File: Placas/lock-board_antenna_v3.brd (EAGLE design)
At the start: 7 parts

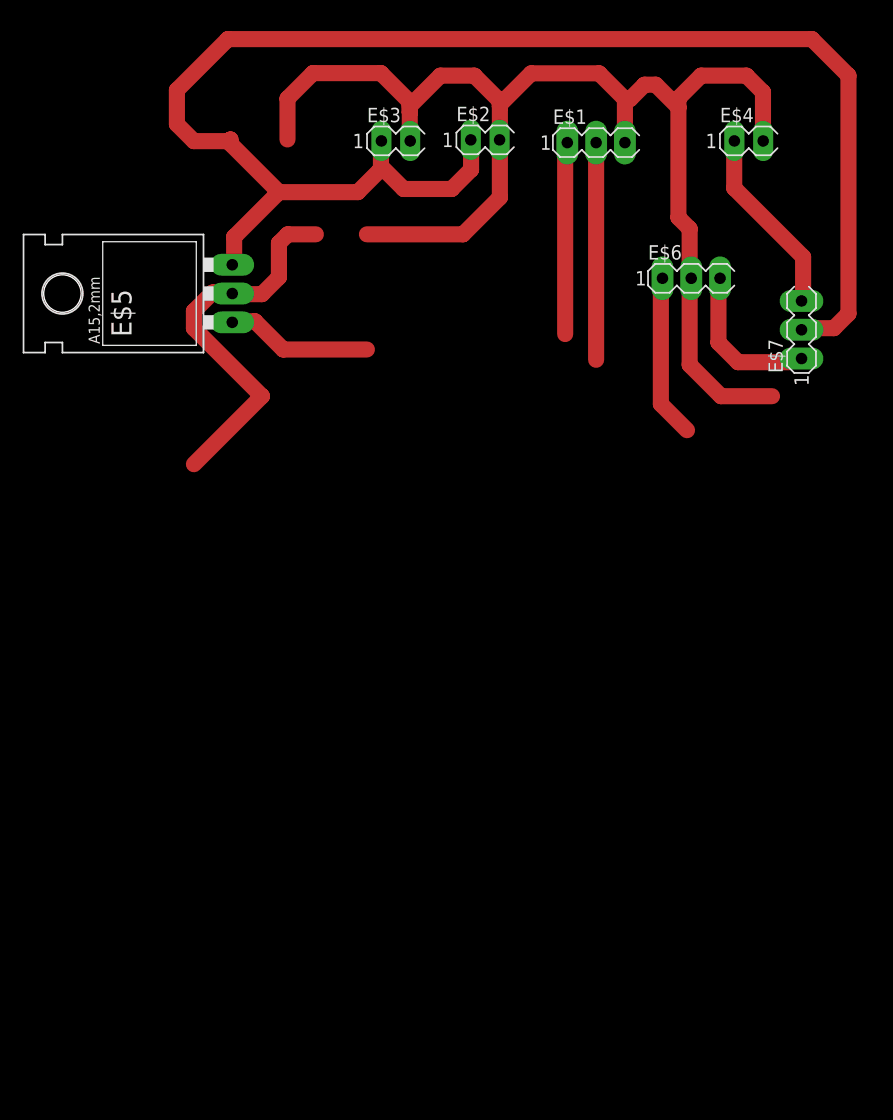
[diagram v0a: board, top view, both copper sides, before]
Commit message: New antenna board
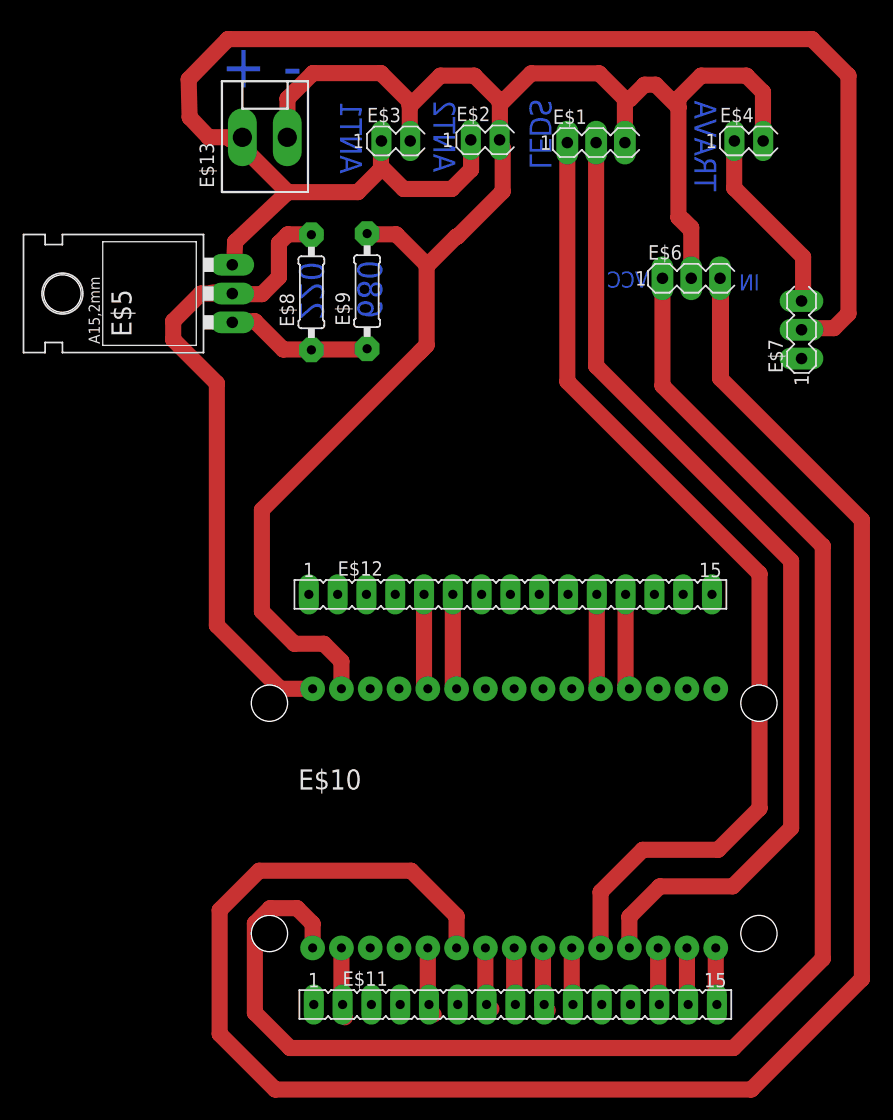
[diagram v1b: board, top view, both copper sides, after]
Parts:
- added E$10: (no value), ESP12E_DEVKIT:ESP12E_DEVKIT
- added E$11, E$12: (no value), con-lsta:FE15
- added E$13: (no value), con-molex:KK-156-2
- added E$8, E$9: (no value), eagle-ltspice:0207/10
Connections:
- new net S$1: E$10.VIN, E$5.2
- new net S$10: E$10.D6, E$11.7
- new net S$11: E$10.D5, E$11.8
- new net S$12: E$10.GND@2, E$11.9
- new net S$13: E$10.3V3@1, E$11.10
- new net S$14: E$10.D2, E$11.13
- new net S$15: E$10.D1, E$11.14
- new net S$16: E$10.D0, E$11.15
- new net S$17: E$10.3V3@0, E$12.5
- new net S$18: E$10.GND@0, E$12.6
- new net S$19: E$10.SD3, E$12.12
- new net S$2: E$2.2
- new net S$20: E$10.SD2, E$12.11
- new net S$21: E$6.2
- new net S$22: E$11.6
- new net S$23: E$10.D7, E$6.3
- new net S$24: E$7.1
- new net S$3: E$10.GND@1
- new net S$4: E$10.3V3@2, E$6.1
- new net S$5: E$1.2, E$10.D3
- new net S$6: E$1.1, E$10.D4
- new net S$7: E$10.GND@3, E$11.2
- new net S$8: E$10.D8, E$11.5
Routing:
- net S$23: track 0.00 -> 177.0 mm
- net S$4: track 0.00 -> 136.8 mm
- net S$5: track 0.00 -> 87.9 mm
- net S$6: track 0.00 -> 87.8 mm
- net S$1: track 0.00 -> 45.4 mm
- net S$3: track 0.00 -> 40.2 mm
- net S$67: track 33.9 -> 13.1 mm
- net S$72: track 19.3 -> 0.00 mm
- net S$71: track 17.0 -> 0.00 mm
- net S$81: track 14.5 -> 0.00 mm
- net S$64: track 12.7 -> 0.00 mm
- net S$68: track 120.6 -> 109.7 mm
- net S$18: track 0.00 -> 8.46 mm
- net S$20: track 0.00 -> 8.46 mm
- net S$19: track 0.00 -> 8.46 mm
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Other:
- board text added: "- +"
- board text added: "220"
- board text added: "680"
- board text added: "ANT1"
- board text added: "ANT2"
- board text added: "IN"
- board text added: "LEDS"
- board text added: "TRAVA"
- board text added: "VCC"
